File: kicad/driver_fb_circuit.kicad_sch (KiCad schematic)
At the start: 69 parts, among them Q1 IRFZ44N, Q2 IRFZ44N, Q3 IRFZ44N, Q4 IRFZ44N, Q5 IRFZ44N, Q6 IRFZ44N, U1 IR2104, U2 INA180A2, U3 INA180A2, U4 INA180A2, U5 IR2104, U6 IR2104

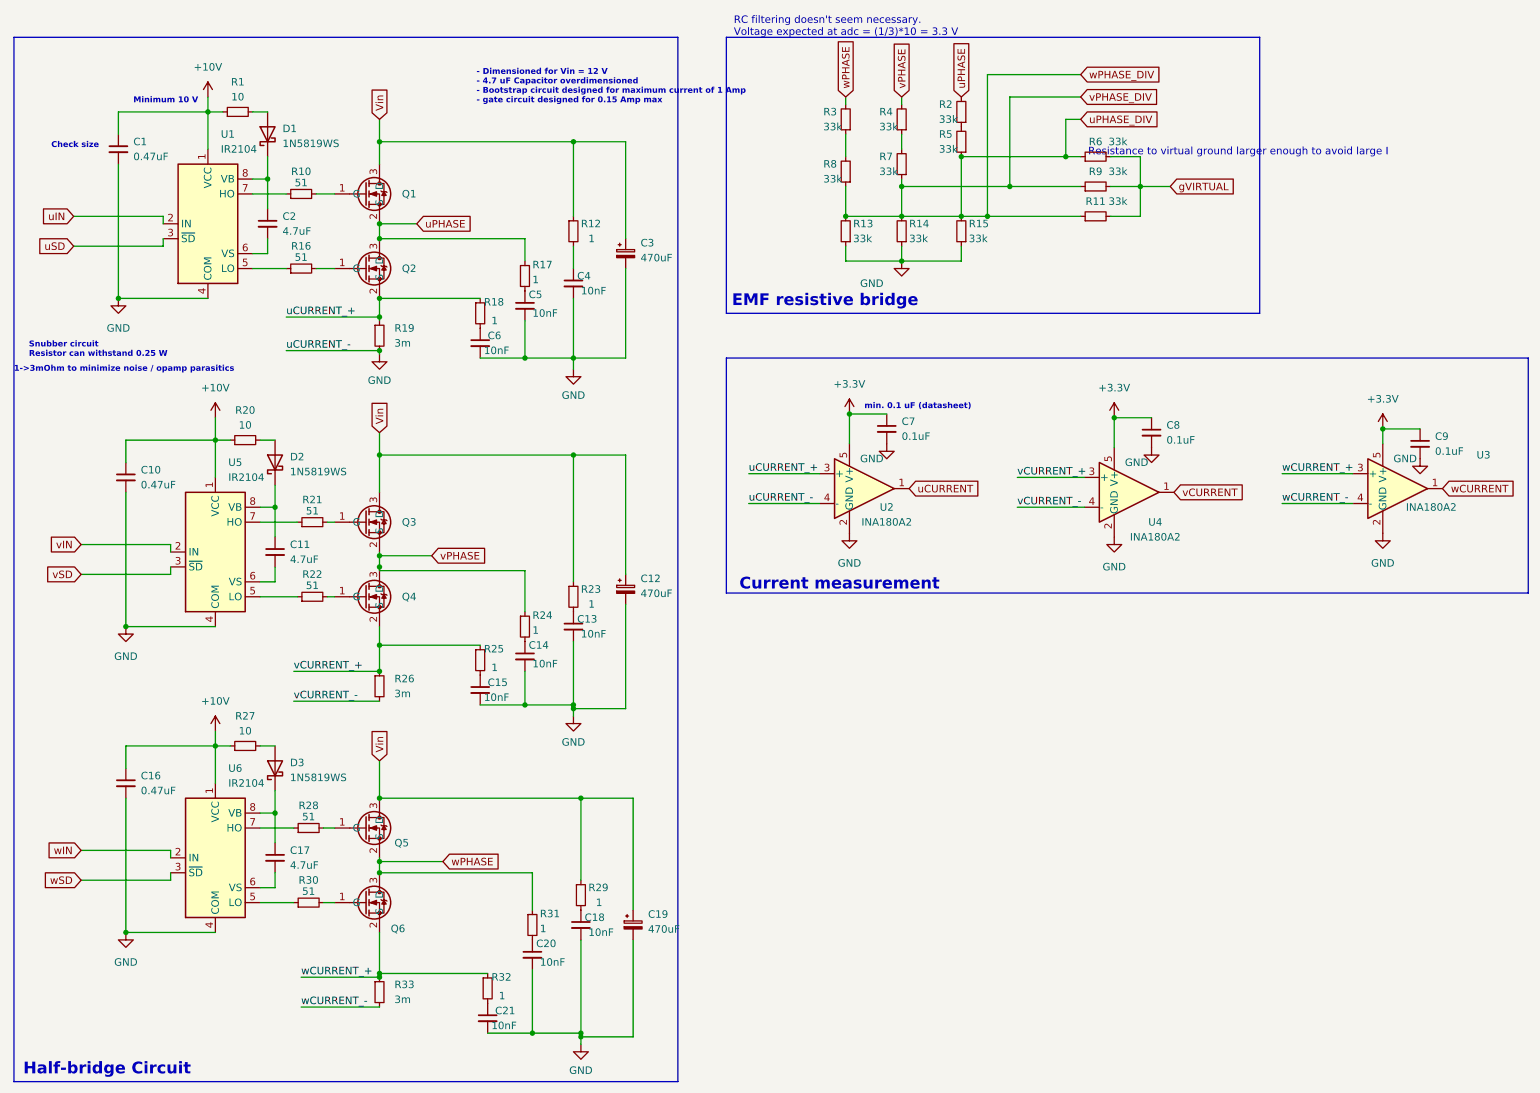
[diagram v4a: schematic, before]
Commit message: [kicad] added soldering pads for phases and battery connectors, rearranged schematic, added tooling holes, fixed ERC errors [scripts] minor footprint calculations
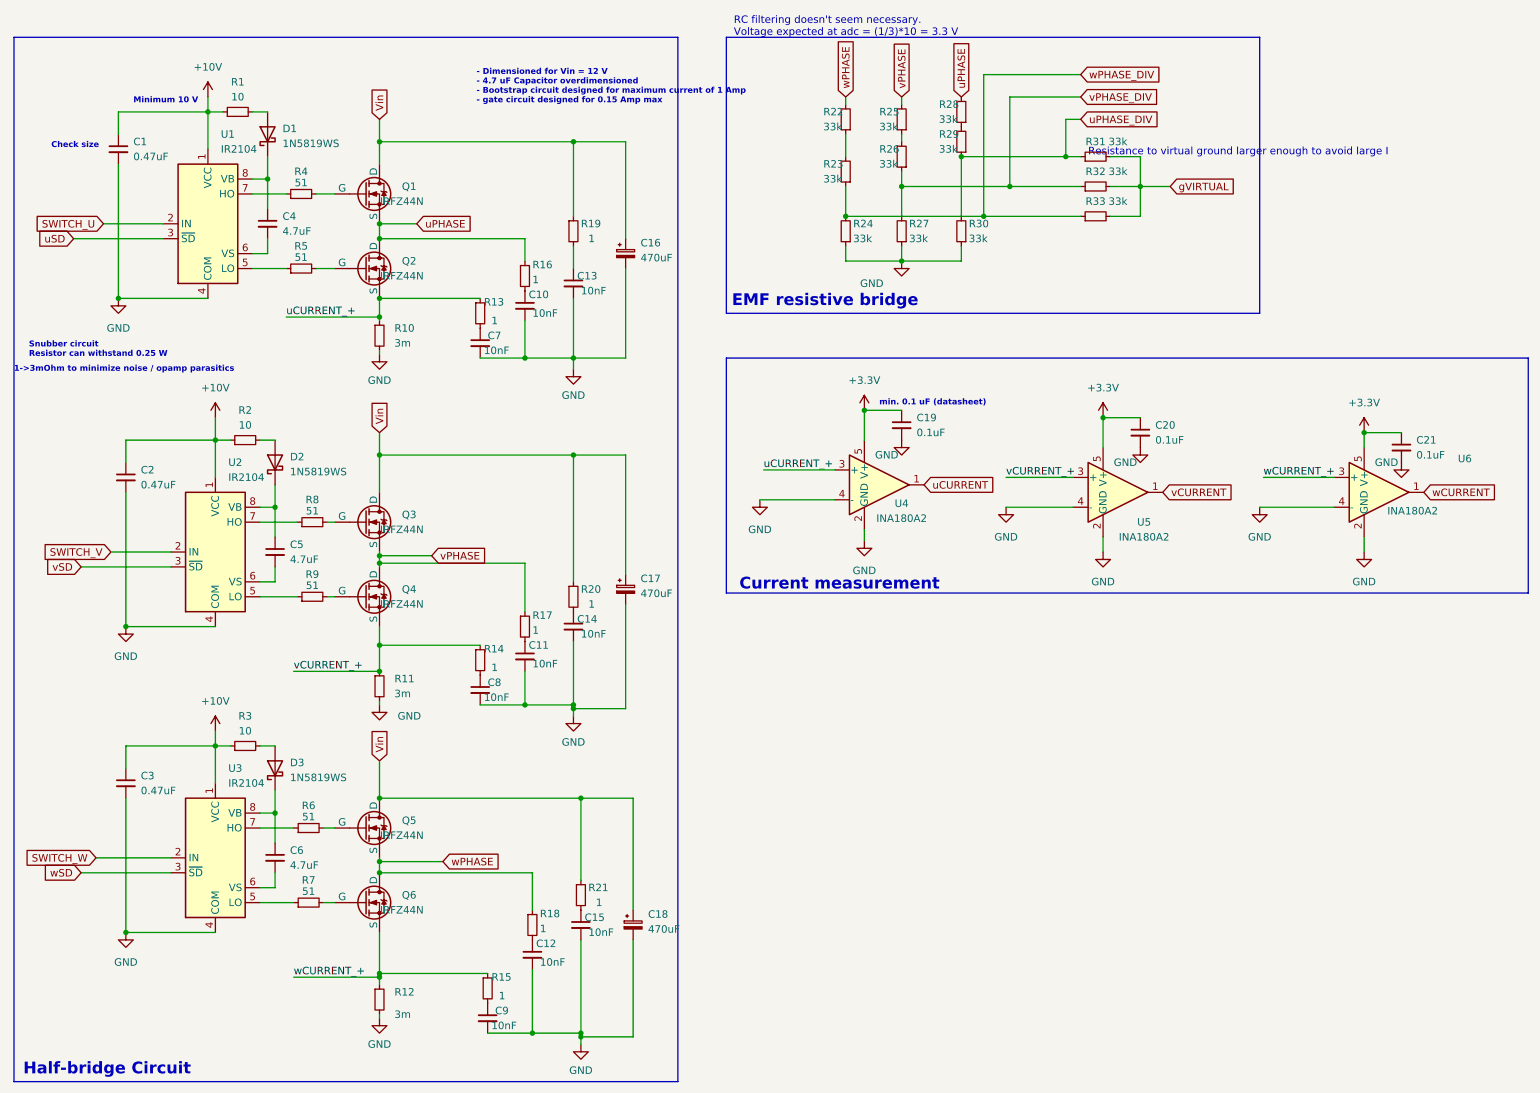
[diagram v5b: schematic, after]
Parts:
- removed Q1, Q2, Q3, Q4, Q5, Q6: IRFZ44N, Package_TO_SOT_THT:TO-220-3_Vertical, symbol bldc_lib:IRFZ44N
- added Q1, Q2, Q3, Q4, Q5, Q6: IRFZ44N, Package_TO_SOT_THT:TO-220-3_Vertical, symbol Simulation_SPICE:NMOS
- renumbered C5 to C10, C14 to C11, C20 to C12, C4 to C13, C13 to C14, C18 to C15, C3 to C16, C12 to C17, C19 to C18, C7 to C19, C10 to C2, C8 to C20, C9 to C21, C16 to C3, C2 to C4, C11 to C5, C17 to C6, C6 to C7, C15 to C8, C21 to C9, R19 to R10, R26 to R11, R33 to R12, R18 to R13, R25 to R14, R32 to R15, R17 to R16, R24 to R17, R31 to R18, R12 to R19, R20 to R2, R23 to R20, R29 to R21, R3 to R22, R8 to R23, R13 to R24, R4 to R25, R7 to R26, R14 to R27, R2 to R28, R5 to R29, R27 to R3, R15 to R30, R6 to R31, R9 to R32, R11 to R33, R10 to R4, R16 to R5, R28 to R6, R30 to R7, R21 to R8, R22 to R9, U5 to U2, U6 to U3, U2 to U4, U4 to U5, U3 to U6
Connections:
- net vCURRENT_- is gone; now on net GND: R11.2, U5.4 (-)
- net wCURRENT_- is gone; now on net GND: R12.2, U6.4 (-)
- net Vin: now also Q1.1 (D), Q3.1 (D), Q5.1 (D)
- net uCURRENT_+: now also Q2.3 (S)
- net uPHASE: now also Q1.3 (S), Q2.1 (D)
- net uPHASE_DIV: no longer R23.1, R24.2, R26.1, R27.2, R32.1, R33.1
- net vCURRENT_+: now also Q4.3 (S)
- net vPHASE: now also Q3.3 (S), Q4.1 (D)
- net wCURRENT_+: now also Q6.3 (S)
- net wPHASE: now also Q5.3 (S), Q6.1 (D)
- net at R7.2: now also Q6.2 (G)
- net at R8.2: now also Q3.2 (G)
- net at R6.2: now also Q5.2 (G)
- net at R4.2: now also Q1.2 (G)
- net at R9.2: now also Q4.2 (G)
- net at R5.2: now also Q2.2 (G)
- net uIN renamed SWITCH_U
- net vIN renamed SWITCH_V
- net wIN renamed SWITCH_W
- new net vPHASE_DIV: R26.1, R27.2, R32.1
- new net wPHASE_DIV: R23.1, R24.2, R33.1
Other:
- company: (none) -> Igor Wolfs
- title: (none) -> BLDC Driver Project
- moved on the sheet: C19, C20, C21, R12, R26, U4, U5, U6
